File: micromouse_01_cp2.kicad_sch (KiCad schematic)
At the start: 36 parts, among them IC2 MPU-6500, IC5 DRV8835DSSR, M1 MK06-4.5, M2 MK06-4.5, U10 MA730, U11 MA730, U13 MCP3464T-E/NC, U9 ESP32-S3-PICO-1-N8R2

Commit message: N8R8用回路（仮）
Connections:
- net ENCL_CS: now also U9.11 (GPIO6); no longer U9.13 (GPIO8)
- net ENC_CLK: now also U9.12 (GPIO7); no longer U9.41 (GPIO36)
- net ENC_MISO: now also U9.13 (GPIO8); no longer U9.40 (GPIO35)
- net ENC_MOSI: now also U9.14 (GPIO9); no longer U9.39 (GPIO34)
- net LED_FR: now also U9.27 (GPIO21); no longer U9.38 (GPIO33)
- net LED_R: now also U9.24 (GPIO18); no longer U9.27 (GPIO21)
- net LED_SCL: now also U9.44 (MTCK); no longer U9.42 (GPIO37)
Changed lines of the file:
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@@
   (no_connect (at 256.54 86.36))
   (no_connect (at 73.66 137.16))
+  (no_connect (at 256.54 76.2))
   (no_connect (at 121.92 45.72))
-  (no_connect (at 256.54 66.04))
-  (no_connect (at 190.5 91.44))
+  (no_connect (at 256.54 73.66))
   (no_connect (at 256.54 40.64))
   (no_connect (at 68.58 106.68))
   (no_connect (at 96.52 43.18))
-  (no_connect (at 190.5 66.04))
   (no_connect (at 60.96 137.16))
   (no_connect (at 71.12 40.64))
@@
   (no_connect (at 71.12 33.02))
   (no_connect (at 71.12 137.16))
+  (no_connect (at 256.54 71.12))
   (no_connect (at 256.54 43.18))
   (no_connect (at 238.76 142.24))
@@
   (no_connect (at 190.5 73.66))
   (no_connect (at 63.5 137.16))
+  (no_connect (at 256.54 78.74))
   (no_connect (at 38.1 119.38))
-  (no_connect (at 190.5 58.42))
   (no_connect (at 256.54 101.6))
   (no_connect (at 48.26 76.2))
@@
   (no_connect (at 121.92 30.48))
   (no_connect (at 256.54 88.9))
-  (no_connect (at 190.5 60.96))
+  (no_connect (at 256.54 81.28))
   (no_connect (at 121.92 40.64))
   (no_connect (at 71.12 106.68))
@@
     (stroke (width 0) (type default))
   )
-  (wire (pts (xy 259.08 76.2) (xy 256.54 76.2))
-    (stroke (width 0) (type default))
-  )
   (wire (pts (xy 109.22 53.34) (xy 109.22 55.88))
     (stroke (width 0) (type default))
@@
     (stroke (width 0) (type default))
   )
-  (wire (pts (xy 259.08 78.74) (xy 256.54 78.74))
-    (stroke (width 0) (type default))
-  )
   (wire (pts (xy 128.27 180.34) (xy 128.27 184.15))
     (stroke (width 0) (type default))
@@
     (stroke (width 0) (type default))
   )
-  (wire (pts (xy 259.08 71.12) (xy 256.54 71.12))
-    (stroke (width 0) (type default))
-  )
   (wire (pts (xy 170.18 132.08) (xy 170.18 143.51))
     (stroke (width 0) (type default))
@@
     (stroke (width 0) (type default))
   )
+  (wire (pts (xy 187.96 91.44) (xy 190.5 91.44))
+    (stroke (width 0) (type default))
+  )
   (wire (pts (xy 30.48 68.58) (xy 30.48 71.12))
     (stroke (width 0) (type default))
@@
     (stroke (width 0) (type default))
   )
+  (wire (pts (xy 187.96 58.42) (xy 190.5 58.42))
+    (stroke (width 0) (type default))
+  )
   (wire (pts (xy 101.6 124.46) (xy 96.52 124.46))
     (stroke (width 0) (type default))
@@
     (stroke (width 0) (type default))
   )
+  (wire (pts (xy 187.96 66.04) (xy 190.5 66.04))
+    (stroke (width 0) (type default))
+  )
   (wire (pts (xy 76.2 22.86) (xy 73.66 22.86))
     (stroke (width 0) (type default))
@@
     (stroke (width 0) (type default))
   )
-  (wire (pts (xy 259.08 81.28) (xy 256.54 81.28))
-    (stroke (width 0) (type default))
-  )
   (wire (pts (xy 58.42 50.8) (xy 58.42 53.34))
     (stroke (width 0) (type default))
@@
     (stroke (width 0) (type default))
   )
+  (wire (pts (xy 256.54 66.04) (xy 259.08 66.04))
+    (stroke (width 0) (type default))
+  )
   (wire (pts (xy 157.48 57.15) (xy 170.18 57.15))
     (stroke (width 0) (type default))
@@
     (stroke (width 0) (type default))
   )
+  (wire (pts (xy 187.96 60.96) (xy 190.5 60.96))
+    (stroke (width 0) (type default))
+  )
   (wire (pts (xy 82.55 102.87) (xy 83.82 102.87))
     (stroke (width 0) (type default))
@@
   )
   (wire (pts (xy 161.29 175.26) (xy 161.29 177.8))
-    (stroke (width 0) (type default))
-  )
-  (wire (pts (xy 259.08 73.66) (xy 256.54 73.66))
     (stroke (width 0) (type default))
   )
@@
     )
   )
+  (global_label "ENC_MOSI" (shape output) (at 187.96 66.04 180) (fields_autoplaced)
+    (effects (font (size 1.27 1.27)) (justify right))
+    (property "Intersheetrefs" "${INTERSHEET_REFS}" (at 175.6615 66.04 0)
+      (effects (font (size 1.27 1.27)) (justify right) hide)
+    )
+  )
   (global_label "LED_SDA" (shape bidirectional) (at 259.08 68.58 0) (fields_autoplaced)
     (effects (font (size 1.27 1.27)) (justify left))
@@
     )
   )
-  (global_label "ENC_MOSI" (shape output) (at 259.08 78.74 0) (fields_autoplaced)
-    (effects (font (size 1.27 1.27)) (justify left))
-    (property "Intersheetrefs" "${INTERSHEET_REFS}" (at 271.3785 78.74 0)
-      (effects (font (size 1.27 1.27)) (justify left) hide)
+  (global_label "ENC_MISO" (shape input) (at 187.96 63.5 180) (fields_autoplaced)
+    (effects (font (size 1.27 1.27)) (justify right))
+    (property "Intersheetrefs" "${INTERSHEET_REFS}" (at 175.6615 63.5 0)
+      (effects (font (size 1.27 1.27)) (justify right) hide)
     )
   )
@@
     )
   )
-  (global_label "ENCL_CS" (shape output) (at 187.96 63.5 180) (fields_autoplaced)
-    (effects (font (size 1.27 1.27)) (justify right))
-    (property "Intersheetrefs" "${INTERSHEET_REFS}" (at 176.7501 63.5 0)
-      (effects (font (size 1.27 1.27)) (justify right) hide)
-    )
-  )
   (global_label "ENCR_CS" (shape input) (at 93.98 38.1 180) (fields_autoplaced)
     (effects (font (size 1.27 1.27)) (justify right))
@@
     )
   )
+  (global_label "ENC_CLK" (shape output) (at 187.96 60.96 180) (fields_autoplaced)
+    (effects (font (size 1.27 1.27)) (justify right))
+    (property "Intersheetrefs" "${INTERSHEET_REFS}" (at 176.6896 60.96 0)
+      (effects (font (size 1.27 1.27)) (justify right) hide)
+    )
+  )
   (global_label "SENS_L" (shape input) (at 167.64 139.7 180) (fields_autoplaced)
     (effects (font (size 1.27 1.27)) (justify right))
@@
     )
   )
+  (global_label "LED_SCL" (shape output) (at 259.08 66.04 0) (fields_autoplaced)
+    (effects (font (size 1.27 1.27)) (justify left))
+    (property "Intersheetrefs" "${INTERSHEET_REFS}" (at 269.9875 66.04 0)
+      (effects (font (size 1.27 1.27)) (justify left) hide)
+    )
+  )
   (global_label "LED_FL" (shape output) (at 187.96 88.9 180) (fields_autoplaced)
     (effects (font (size 1.27 1.27)) (justify right))
@@
     )
   )
-  (global_label "ENC_MISO" (shape input) (at 259.08 76.2 0) (fields_autoplaced)
-    (effects (font (size 1.27 1.27)) (justify left))
-    (property "Intersheetrefs" "${INTERSHEET_REFS}" (at 271.3785 76.2 0)
-      (effects (font (size 1.27 1.27)) (justify left) hide)
-    )
-  )
   (global_label "ENC_MISO" (shape output) (at 43.18 33.02 180) (fields_autoplaced)
     (effects (font (size 1.27 1.27)) (justify right))
@@
     )
   )
-  (global_label "LED_SCL" (shape output) (at 259.08 71.12 0) (fields_autoplaced)
-    (effects (font (size 1.27 1.27)) (justify left))
-    (property "Intersheetrefs" "${INTERSHEET_REFS}" (at 269.9875 71.12 0)
-      (effects (font (size 1.27 1.27)) (justify left) hide)
+  (global_label "LED_FR" (shape output) (at 187.96 99.06 180) (fields_autoplaced)
+    (effects (font (size 1.27 1.27)) (justify right))
+    (property "Intersheetrefs" "${INTERSHEET_REFS}" (at 178.2015 99.06 0)
+      (effects (font (size 1.27 1.27)) (justify right) hide)
     )
   )
@@
     )
   )
-  (global_label "LED_FR" (shape output) (at 259.08 81.28 0) (fields_autoplaced)
-    (effects (font (size 1.27 1.27)) (justify left))
-    (property "Intersheetrefs" "${INTERSHEET_REFS}" (at 268.8385 81.28 0)
-      (effects (font (size 1.27 1.27)) (justify left) hide)
+  (global_label "ENCL_CS" (shape output) (at 187.96 58.42 180) (fields_autoplaced)
+    (effects (font (size 1.27 1.27)) (justify right))
+    (property "Intersheetrefs" "${INTERSHEET_REFS}" (at 176.7501 58.42 0)
+      (effects (font (size 1.27 1.27)) (justify right) hide)
     )
   )
@@
     )
   )
-  (global_label "ENC_CLK" (shape output) (at 259.08 73.66 0) (fields_autoplaced)
-    (effects (font (size 1.27 1.27)) (justify left))
-    (property "Intersheetrefs" "${INTERSHEET_REFS}" (at 270.3504 73.66 0)
-      (effects (font (size 1.27 1.27)) (justify left) hide)
-    )
-  )
   (global_label "ADC_CS" (shape input) (at 241.3 152.4 0) (fields_autoplaced)
     (effects (font (size 1.27 1.27)) (justify left))
@@
     )
   )
-  (global_label "LED_R" (shape output) (at 187.96 99.06 180) (fields_autoplaced)
-    (effects (font (size 1.27 1.27)) (justify right))
-    (property "Intersheetrefs" "${INTERSHEET_REFS}" (at 179.2901 99.06 0)
-      (effects (font (size 1.27 1.27)) (justify right) hide)
-    )
-  )
   (global_label "MOT1_PHASE" (shape output) (at 259.08 58.42 0) (fields_autoplaced)
     (effects (font (size 1.27 1.27)) (justify left))
@@
     )
   )
+  (global_label "LED_R" (shape output) (at 187.96 91.44 180) (fields_autoplaced)
+    (effects (font (size 1.27 1.27)) (justify right))
+    (property "Intersheetrefs" "${INTERSHEET_REFS}" (at 179.2901 91.44 0)
+      (effects (font (size 1.27 1.27)) (justify right) hide)
+    )
+  )

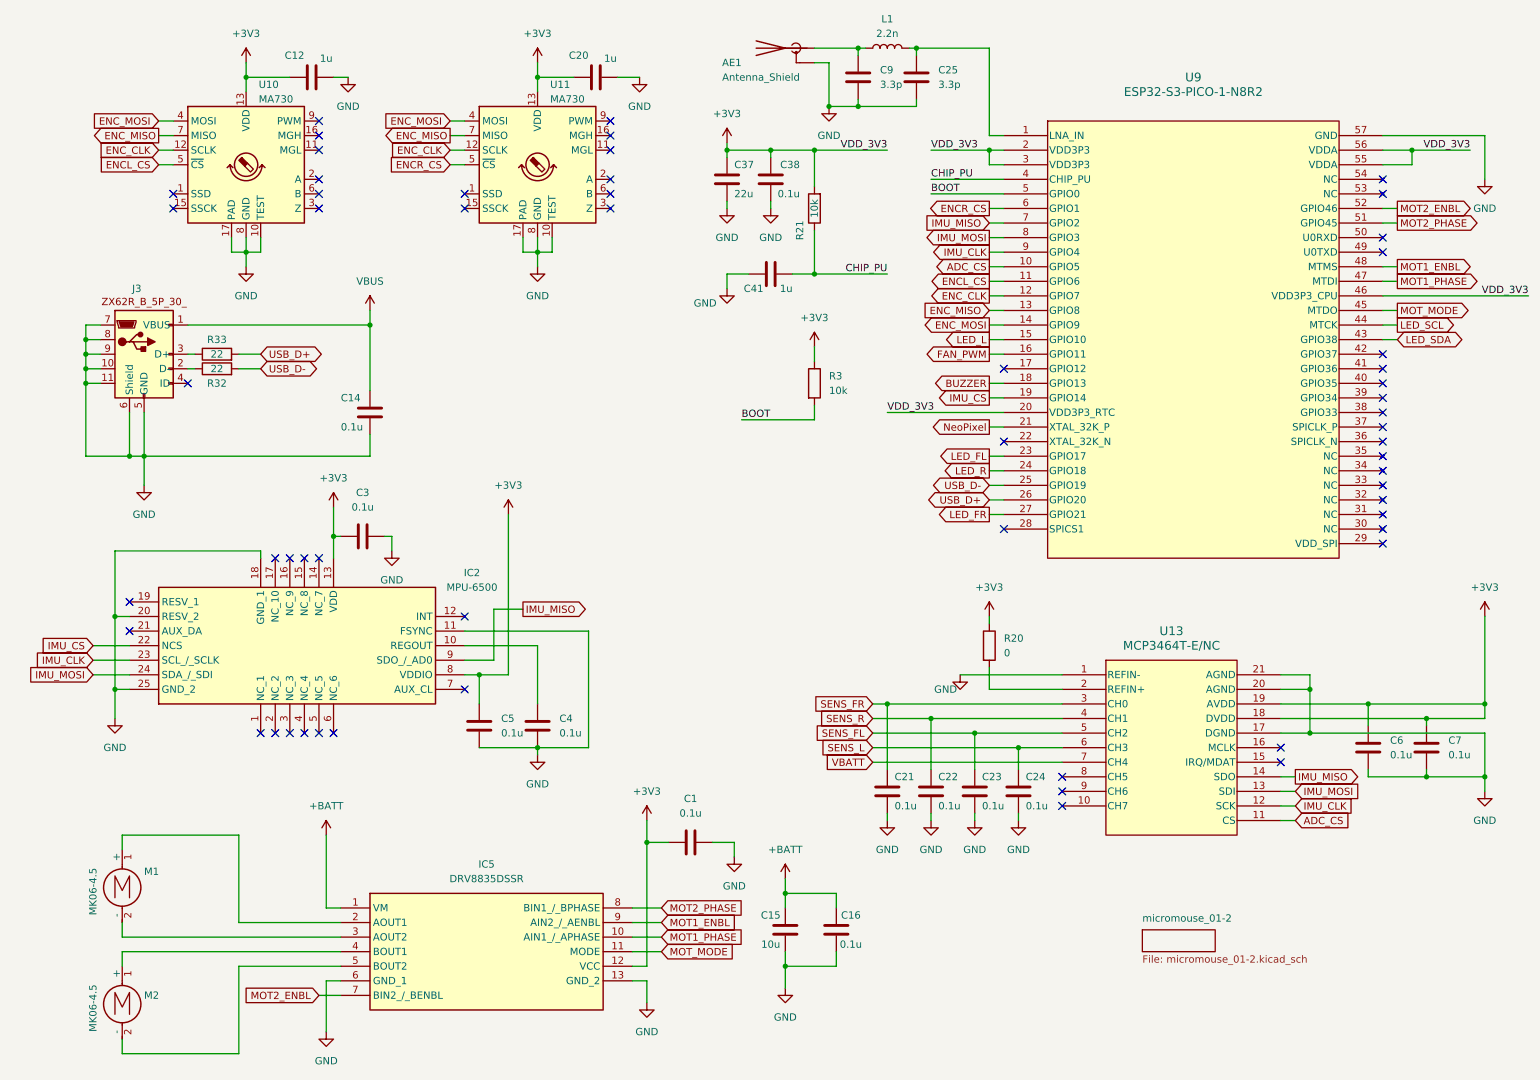
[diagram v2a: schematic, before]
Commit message: [update]ADCと壁センサ周りを変更
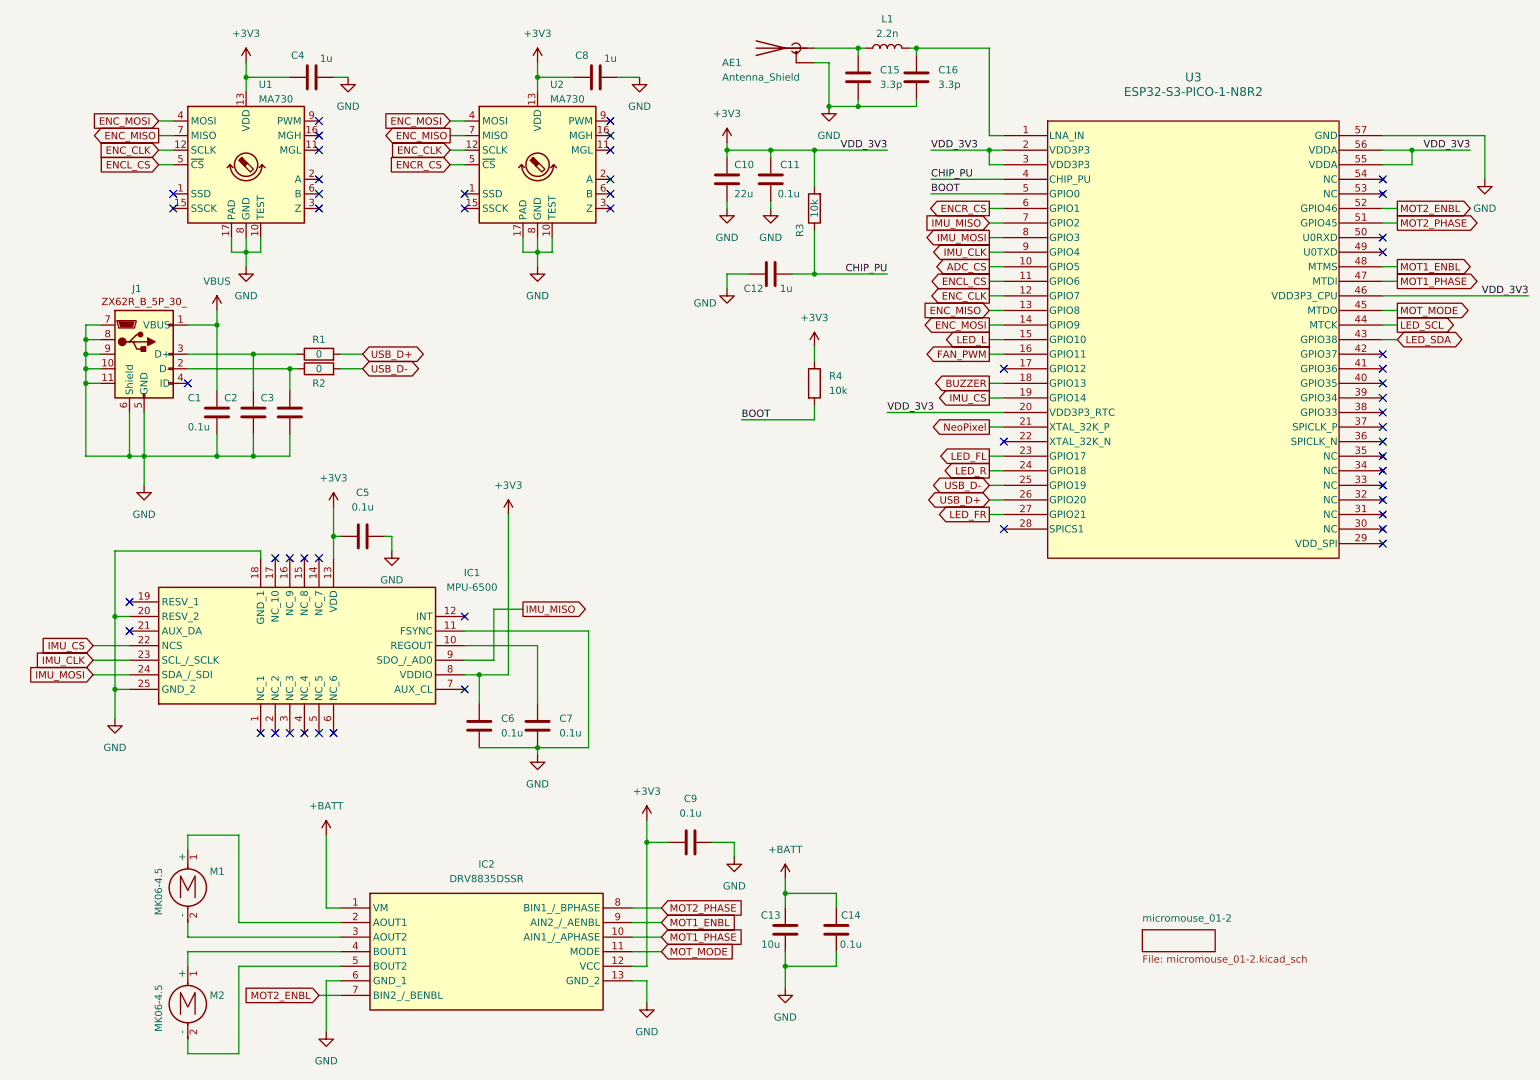
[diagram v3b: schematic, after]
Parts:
- removed C21, C22, C23, C24, C6, C7: 0.1u, Capacitor_SMD:C_0402_1005Metric, symbol Device:C
- removed R20: 0, Resistor_SMD:R_0402_1005Metric, symbol Device:R
- removed U13: MCP3464T-E/NC, UQFN20_NC_MCH, symbol 2024-03-13_05-36-02:MCP3464T-E_NC
- added C2, C3: ~, Capacitor_SMD:C_0402_1005Metric, symbol Device:C
- R1: renamed from R33; value 22 -> 0
- R2: renamed from R32; value 22 -> 0
- renumbered C14 to C1, C37 to C10, C38 to C11, C41 to C12, C15 to C13, C16 to C14, C9 to C15, C25 to C16, C12 to C4, C3 to C5, C5 to C6, C4 to C7, C20 to C8, C1 to C9, IC2 to IC1, IC5 to IC2, J3 to J1, R21 to R3, R3 to R4, U10 to U1, U11 to U2, U9 to U3
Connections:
- net GND: now also C2.2, C3.2
- net at J1.2 (D-), R2.1: now also C3.1
- net at J1.3 (D+), R1.1: now also C2.1
- no-connect marks 57 -> 52
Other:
- moved on the sheet: C1, M1, M2, R1, R2

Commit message: 新しい部品乗せた
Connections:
- net IMU_CLK: now also U3.8 (GPIO3); no longer U3.9 (GPIO4)
- net IMU_MISO: now also U3.9 (GPIO4); no longer U3.7 (GPIO2)
- net IMU_MOSI: now also U3.7 (GPIO2); no longer U3.8 (GPIO3)
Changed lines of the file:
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@@
     )
   )
-  (global_label "IMU_MOSI" (shape output) (at 187.96 50.8 180) (fields_autoplaced)
+  (global_label "IMU_MISO" (shape input) (at 187.96 53.34 180) (fields_autoplaced)
     (effects (font (size 1.27 1.27)) (justify right))
-    (property "Intersheetrefs" "${INTERSHEET_REFS}" (at 176.0243 50.8 0)
+    (property "Intersheetrefs" "${INTERSHEET_REFS}" (at 176.0243 53.34 0)
       (effects (font (size 1.27 1.27)) (justify right) hide)
     )
@@
     )
   )
-  (global_label "IMU_CLK" (shape output) (at 187.96 53.34 180) (fields_autoplaced)
-    (effects (font (size 1.27 1.27)) (justify right))
-    (property "Intersheetrefs" "${INTERSHEET_REFS}" (at 177.0524 53.34 0)
-      (effects (font (size 1.27 1.27)) (justify right) hide)
-    )
-  )
   (global_label "MOT_MODE" (shape input) (at 130.81 175.26 0) (fields_autoplaced)
     (effects (font (size 1.27 1.27)) (justify left))
     (property "Intersheetrefs" "${INTERSHEET_REFS}" (at 143.7132 175.26 0)
       (effects (font (size 1.27 1.27)) (justify left) hide)
+    )
+  )
+  (global_label "IMU_CLK" (shape output) (at 187.96 50.8 180) (fields_autoplaced)
+    (effects (font (size 1.27 1.27)) (justify right))
+    (property "Intersheetrefs" "${INTERSHEET_REFS}" (at 177.0524 50.8 0)
+      (effects (font (size 1.27 1.27)) (justify right) hide)
     )
   )
@@
     )
   )
-  (global_label "IMU_MISO" (shape input) (at 187.96 48.26 180) (fields_autoplaced)
-    (effects (font (size 1.27 1.27)) (justify right))
-    (property "Intersheetrefs" "${INTERSHEET_REFS}" (at 176.0243 48.26 0)
-      (effects (font (size 1.27 1.27)) (justify right) hide)
-    )
-  )
   (global_label "USB_D-" (shape bidirectional) (at 187.96 93.98 180) (fields_autoplaced)
     (effects (font (size 1.27 1.27)) (justify right))
@@
     )
   )
+  (global_label "IMU_MOSI" (shape output) (at 187.96 48.26 180) (fields_autoplaced)
+    (effects (font (size 1.27 1.27)) (justify right))
+    (property "Intersheetrefs" "${INTERSHEET_REFS}" (at 176.0243 48.26 0)
+      (effects (font (size 1.27 1.27)) (justify right) hide)
+    )
+  )

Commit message: Initial Commit
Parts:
- removed AE1: Antenna_Shield, RF_Antenna:Texas_SWRA117D_2.4GHz_Right, symbol Device:Antenna_Shield
- removed C15, C16: 3.3p, Capacitor_SMD:C_0402_1005Metric, symbol Device:C
- removed L1: 2.2n, Inductor_SMD:L_0402_1005Metric, symbol Device:L
- removed U3: ESP32-S3-PICO-1-N8R2, QFN56_7X7_EXP, symbol 2024-02-29_13-39-39:ESP32-S3-PICO-1-N8R2
- added U12: ESP32-S3-MINI-1-N8, footprints:XCVR_ESP32-S3-MINI-1-N8, symbol ESP32-S3-MINI-1-N8:ESP32-S3-MINI-1-N8
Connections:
- net +3V3: now also U12.3 (3V3)
- net ADC_CS: now also U12.9 (IO5)
- net BOOT: now also U12.4 (IO0)
- net BUZZER: now also U12.17 (IO13)
- net ENCL_CS: now also U12.10 (IO6)
- net ENCR_CS: now also U12.5 (IO1)
- net ENC_CLK: now also U12.11 (IO7)
- net ENC_MISO: now also U12.12 (IO8)
- net ENC_MOSI: now also U12.13 (IO9)
- net FAN_PWM: now also U12.15 (IO11)
- net GND: now also U12.1 (GND), U12.2 (GND__1), U12.42 (GND__2), U12.43 (GND__3), U12.46 (GND__4), U12.47 (GND__5), U12.48 (GND__6), U12.49 (GND__7), U12.50 (GND__8), U12.51 (GND__9), U12.52 (GND__10), U12.53 (GND__11), U12.54 (GND__12), U12.55 (GND__13), U12.56 (GND__14), U12.57 (GND__15), U12.58 (GND__16), U12.59 (GND__17), U12.60 (GND__18), U12.61 (GND__19), U12.61_1 (GND__20), U12.61_2 (GND__21), U12.61_3 (GND__22), U12.61_4 (GND__23), U12.61_5 (GND__24), U12.61_6 (GND__25), U12.61_7 (GND__26), U12.61_8 (GND__27), U12.62 (GND__28), U12.63 (GND__29), U12.64 (GND__30), U12.65 (GND__31)
- net IMU_CLK: now also U12.7 (IO3)
- net IMU_CS: now also U12.18 (IO14)
- net IMU_MISO: now also U12.8 (IO4)
- net IMU_MOSI: now also U12.6 (IO2)
- net LED_FL: now also U12.21 (IO17)
- net LED_FR: now also U12.25 (IO21)
- net LED_L: now also U12.14 (IO10)
- net LED_R: now also U12.22 (IO18)
- net LED_SCL: now also U12.35 (IO39)
- net LED_SDA: now also U12.34 (IO38)
- net MOT1_ENBL: now also U12.38 (IO42)
- net MOT1_PHASE: now also U12.37 (IO41)
- net MOT2_ENBL: now also U12.44 (IO46)
- net MOT2_PHASE: now also U12.41 (IO45)
- net MOT_MODE: now also U12.36 (IO40)
- net NeoPixel: now also U12.19 (IO15)
- net USB_D+: now also U12.24 (IO20)
- net USB_D-: now also U12.23 (IO19)
- net CHIP_PU renamed EN
- net EN: now also U12.45 (EN)
- no-connect marks 52 -> 43
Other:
- moved on the sheet: C10, C11, C12, R3, R4
